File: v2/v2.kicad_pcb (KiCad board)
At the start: 2 copper layers, 10.6 x 5.5 mm, 63 parts, among them SW1 SW_Push, SW10 SW_Push, SW11 SW_Push, SW12 SW_Push, SW13 SW_Push, SW14 SW_Push, SW15 SW_Push, SW16 SW_Push, SW17 SW_Push, SW18 SW_Push, SW19 SW_Push, SW2 SW_Push, SW20 SW_Push, SW21 SW_Push, SW22 SW_Push, SW23 SW_Push, SW24 SW_Push, SW25 SW_Push, SW26 SW_Push, SW27 SW_Push, SW28 SW_Push, SW29 SW_Push, SW3 SW_Push, SW30 SW_Push, SW31 SW_Push, SW4 SW_Push, SW5 SW_Push, SW6 SW_Push, SW7 SW_Push, SW8 SW_Push, SW9 SW_Push

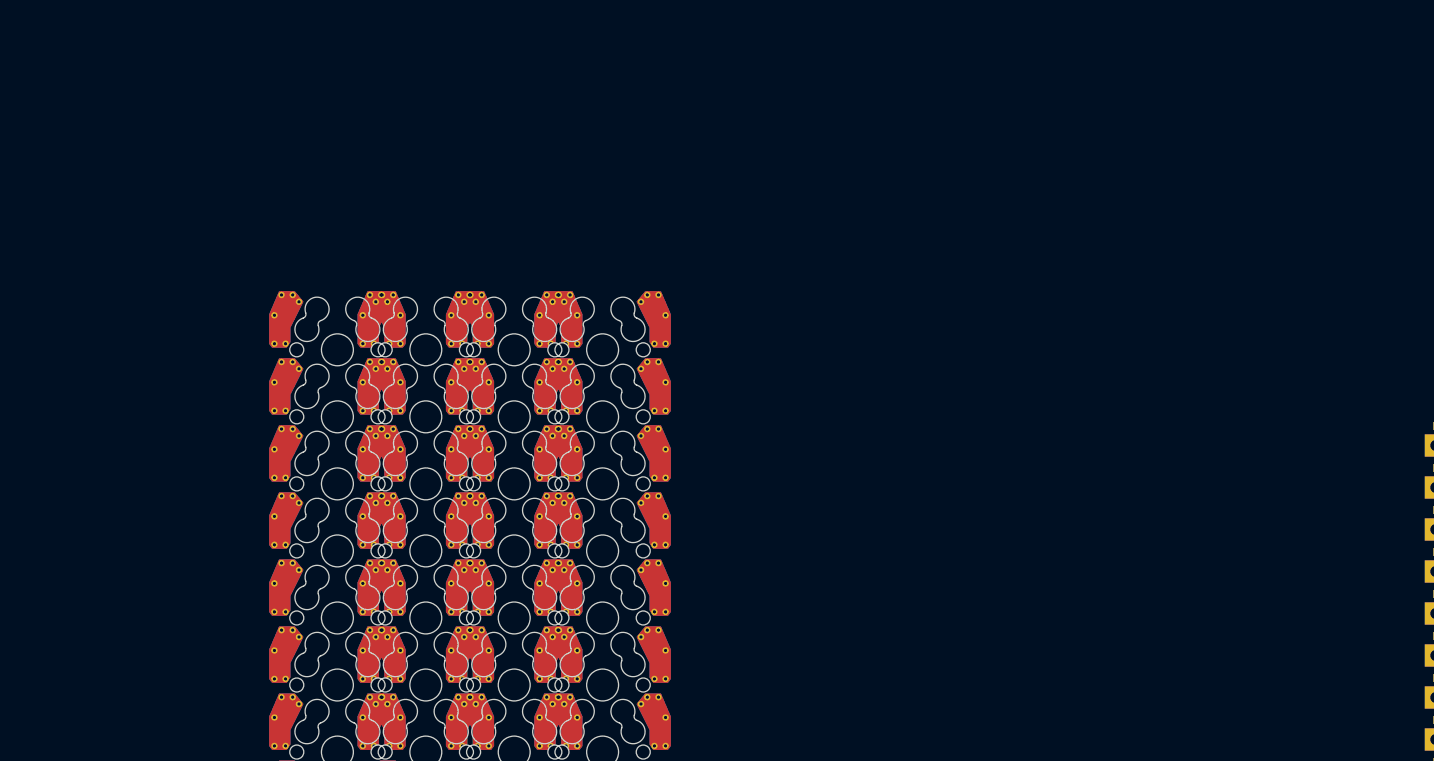
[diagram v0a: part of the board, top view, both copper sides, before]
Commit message: started adding backlighting
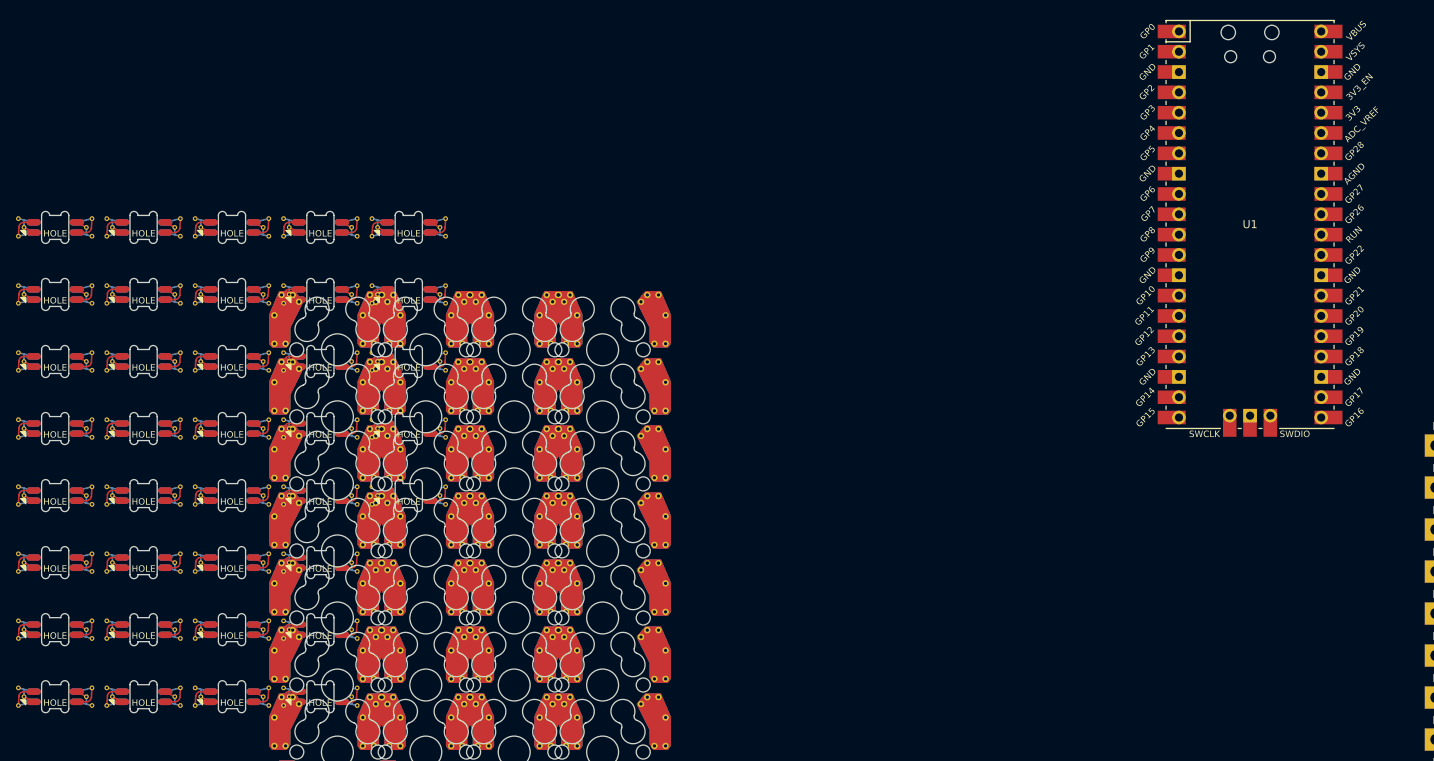
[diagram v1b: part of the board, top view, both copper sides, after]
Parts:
- added D33: SK6812MINI, reversible-kicad-footprints:MX-1U-SK6812Mini-E, F.Cu at (28.8, 34.7)
- added D34: SK6812MINI, reversible-kicad-footprints:MX-1U-SK6812Mini-E, F.Cu at (28.8, 43.0)
- added D35: SK6812MINI, reversible-kicad-footprints:MX-1U-SK6812Mini-E, F.Cu at (28.8, 51.4)
- added D36: SK6812MINI, reversible-kicad-footprints:MX-1U-SK6812Mini-E, F.Cu at (28.8, 59.8)
- added D37: SK6812MINI, reversible-kicad-footprints:MX-1U-SK6812Mini-E, F.Cu at (28.8, 68.2)
- added D38: SK6812MINI, reversible-kicad-footprints:MX-1U-SK6812Mini-E, F.Cu at (28.8, 76.6)
- added D39: SK6812MINI, reversible-kicad-footprints:MX-1U-SK6812Mini-E, F.Cu at (28.8, 84.9)
- added D40: SK6812MINI, reversible-kicad-footprints:MX-1U-SK6812Mini-E, F.Cu at (28.8, 93.3)
- added D41: SK6812MINI, reversible-kicad-footprints:MX-1U-SK6812Mini-E, F.Cu at (39.8, 34.7)
- added D42: SK6812MINI, reversible-kicad-footprints:MX-1U-SK6812Mini-E, F.Cu at (39.8, 43.0)
- added D43: SK6812MINI, reversible-kicad-footprints:MX-1U-SK6812Mini-E, F.Cu at (39.8, 51.4)
- added D44: SK6812MINI, reversible-kicad-footprints:MX-1U-SK6812Mini-E, F.Cu at (39.8, 59.8)
- added D45: SK6812MINI, reversible-kicad-footprints:MX-1U-SK6812Mini-E, F.Cu at (39.8, 68.2)
- added D46: SK6812MINI, reversible-kicad-footprints:MX-1U-SK6812Mini-E, F.Cu at (39.8, 76.6)
- added D47: SK6812MINI, reversible-kicad-footprints:MX-1U-SK6812Mini-E, F.Cu at (39.8, 84.9)
- added D48: SK6812MINI, reversible-kicad-footprints:MX-1U-SK6812Mini-E, F.Cu at (39.8, 93.3)
- added D49: SK6812MINI, reversible-kicad-footprints:MX-1U-SK6812Mini-E, F.Cu at (50.9, 34.7)
- added D50: SK6812MINI, reversible-kicad-footprints:MX-1U-SK6812Mini-E, F.Cu at (50.9, 43.0)
- added D51: SK6812MINI, reversible-kicad-footprints:MX-1U-SK6812Mini-E, F.Cu at (50.9, 51.4)
- added D52: SK6812MINI, reversible-kicad-footprints:MX-1U-SK6812Mini-E, F.Cu at (50.9, 59.8)
- added D53: SK6812MINI, reversible-kicad-footprints:MX-1U-SK6812Mini-E, F.Cu at (50.9, 68.2)
- added D54: SK6812MINI, reversible-kicad-footprints:MX-1U-SK6812Mini-E, F.Cu at (50.9, 76.6)
- added D55: SK6812MINI, reversible-kicad-footprints:MX-1U-SK6812Mini-E, F.Cu at (50.9, 84.9)
- added D56: SK6812MINI, reversible-kicad-footprints:MX-1U-SK6812Mini-E, F.Cu at (50.9, 93.3)
- added D57: SK6812MINI, reversible-kicad-footprints:MX-1U-SK6812Mini-E, F.Cu at (61.9, 34.7)
- added D58: SK6812MINI, reversible-kicad-footprints:MX-1U-SK6812Mini-E, F.Cu at (61.9, 43.0)
- added D59: SK6812MINI, reversible-kicad-footprints:MX-1U-SK6812Mini-E, F.Cu at (61.9, 51.4)
- added D60: SK6812MINI, reversible-kicad-footprints:MX-1U-SK6812Mini-E, F.Cu at (61.9, 59.8)
- added D61: SK6812MINI, reversible-kicad-footprints:MX-1U-SK6812Mini-E, F.Cu at (61.9, 68.2)
- added D62: SK6812MINI, reversible-kicad-footprints:MX-1U-SK6812Mini-E, F.Cu at (61.9, 76.6)
- added D63: SK6812MINI, reversible-kicad-footprints:MX-1U-SK6812Mini-E, F.Cu at (61.9, 84.9)
- added D64: SK6812MINI, reversible-kicad-footprints:MX-1U-SK6812Mini-E, F.Cu at (61.9, 93.3)
- added D65: SK6812MINI, reversible-kicad-footprints:MX-1U-SK6812Mini-E, F.Cu at (73.0, 34.7)
- added D66: SK6812MINI, reversible-kicad-footprints:MX-1U-SK6812Mini-E, F.Cu at (73.0, 43.0)
- added D67: SK6812MINI, reversible-kicad-footprints:MX-1U-SK6812Mini-E, F.Cu at (73.0, 51.4)
- added D68: SK6812MINI, reversible-kicad-footprints:MX-1U-SK6812Mini-E, F.Cu at (73.0, 59.8)
- added D69: SK6812MINI, reversible-kicad-footprints:MX-1U-SK6812Mini-E, F.Cu at (73.0, 68.2)
- added U1: Pico, RPi_Pico:RPi_Pico_SMD_TH, F.Cu at (178.1, 39.4)
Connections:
- D32 pad 1: unconnected-(D32-DOUT-Pad1) -> Net-(D32-DOUT)
- D32 pad 2: unconnected-(D32-VSS-Pad2) -> GND
- D32 pad 4: unconnected-(D32-VDD-Pad4) -> VBUS

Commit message: did some layout using a plugin
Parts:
- removed D36, D41, D47, D53, D59, D65: SK6812MINI, reversible-kicad-footprints:MX-1U-SK6812Mini-E
- added D28: D, Diode_THT:D_5W_P10.16mm_Horizontal, B.Cu at (195.1, 174.2)
- added SW28: SW_Push, reversible-kicad-footprints:MX-1U-Hotswap, F.Cu at (190.2, 169.2)
- D1: moved to B.Cu
- D10: renamed from D11; moved to B.Cu
- D11: renamed from D16; moved to B.Cu
- D12: renamed from D21; moved to B.Cu
- D13: renamed from D26; moved to B.Cu
- D14: renamed from D30; moved to B.Cu
- D15: renamed from D3; moved to B.Cu
- D16: renamed from D7; moved to B.Cu
- D17: renamed from D12; moved to B.Cu
- D18: renamed from D17; moved to B.Cu
- D19: renamed from D22; moved to B.Cu
- D2: renamed from D5; moved to B.Cu
- D20: renamed from D27; moved to B.Cu
- D21: renamed from D31; moved to B.Cu
- D22: renamed from D4; moved to B.Cu
- D23: renamed from D8; moved to B.Cu
- D24: renamed from D13; moved to B.Cu
- D25: renamed from D18; moved to B.Cu
- D26: renamed from D23; moved to B.Cu
- D27: renamed from D28; moved to B.Cu
- D29: renamed from D9; moved to B.Cu
- D3: renamed from D10; moved to B.Cu
- D30: renamed from D14; moved to B.Cu
- D31: renamed from D19; moved to B.Cu
- D32: renamed from D24; moved to B.Cu
- D4: renamed from D15; moved to B.Cu
- D5: renamed from D20; moved to B.Cu
- D6: renamed from D25; moved to B.Cu
- D7: renamed from D29; moved to B.Cu
- D8: renamed from D2; moved to B.Cu
- D9: renamed from D6; moved to B.Cu
- LED1: renamed from D32; moved to B.Cu
- LED10: renamed from D56; moved to B.Cu
- LED11: renamed from D50; moved to B.Cu
- LED12: renamed from D44; moved to B.Cu
- LED13: renamed from D38; moved to B.Cu
- LED14: renamed from D33; moved to B.Cu
- LED15: renamed from D34; moved to B.Cu
- LED16: renamed from D39; moved to B.Cu
- LED17: renamed from D45; moved to B.Cu
- LED18: renamed from D51; moved to B.Cu
- LED19: renamed from D57; moved to B.Cu
- LED2: renamed from D37; moved to B.Cu
- LED20: renamed from D63; moved to B.Cu
- LED21: renamed from D68; moved to B.Cu
- LED22: renamed from D69; moved to B.Cu
- LED23: renamed from D64; moved to B.Cu
- LED24: renamed from D58; moved to B.Cu
- LED25: renamed from D52; moved to B.Cu
- LED26: renamed from D46; moved to B.Cu
- LED27: renamed from D40; moved to B.Cu
- LED28: renamed from D35; moved to B.Cu
- LED29: renamed from D42; moved to B.Cu
- LED3: renamed from D43; moved to B.Cu
- LED30: renamed from D48; moved to B.Cu
- LED31: renamed from D54; moved to B.Cu
- LED32: renamed from D60; moved to B.Cu
- LED4: renamed from D49; moved to B.Cu
- LED5: renamed from D55; moved to B.Cu
- LED6: renamed from D61; moved to B.Cu
- LED7: renamed from D66; moved to B.Cu
- LED8: renamed from D67; moved to B.Cu
- LED9: renamed from D62; moved to B.Cu
- moved LED32 225.9 mm to (233.1, 207.2), turned to 149 degrees
- moved LED31 203.2 mm to (213.6, 198.3), turned to 159 degrees
- moved LED28 199.8 mm to (190.2, 169.2), turned to 179.5 degrees
- moved LED29 197.9 mm to (171.3, 190.9), turned to 174 degrees
- moved LED13 185.4 mm to (210.2, 114.7), turned to 179 degrees
- moved LED25 183.9 mm to (209.5, 152.8), turned to 179 degrees
- moved LED30 182.7 mm to (192.7, 193.4), turned to 169 degrees
- moved SW31 179.6 mm to (213.6, 198.3), turned to -21 degrees
- moved LED19 178.1 mm to (209.8, 133.7), turned to 179 degrees
- moved SW29 166.5 mm to (171.3, 190.9), turned to -6 degrees
- moved LED15 166.3 mm to (171.5, 128.5), turned to 179.5 degrees
- moved LED17 163.3 mm to (190.5, 131.1), turned to 179.5 degrees
- moved LED27 160.1 mm to (171.1, 166.6), turned to 179.5 degrees
- moved LED14 156.6 mm to (152.4, 130.8), turned to 179.5 degrees
- moved LED11 155.9 mm to (190.7, 112.0), turned to 179.5 degrees
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- renumbered SW11 to SW10, SW16 to SW11, SW21 to SW12, SW26 to SW13, SW30 to SW14, SW3 to SW15, SW7 to SW16, SW12 to SW17, SW17 to SW18, SW22 to SW19, SW5 to SW2, SW27 to SW20, SW31 to SW21, SW4 to SW22, SW8 to SW23, SW13 to SW24, SW18 to SW25, SW23 to SW26, SW28 to SW27, SW9 to SW29, SW10 to SW3, SW14 to SW30, SW19 to SW31, SW24 to SW32, SW15 to SW4, SW20 to SW5, SW25 to SW6, SW29 to SW7, SW2 to SW8, SW6 to SW9
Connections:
- LED22 pad 1: Net-(D36-DIN) -> Net-(LED22-DOUT)
- LED29 pad 1: Net-(D42-DOUT) -> unconnected-(LED29-DOUT-Pad1)
- LED29 pad 3: Net-(D42-DIN) -> Net-(LED22-DOUT)
- LED30 pad 1: Net-(D48-DOUT) -> unconnected-(LED30-DOUT-Pad1)
- LED30 pad 3: Net-(D42-DOUT) -> unconnected-(LED30-DIN-Pad3)
- LED31 pad 3: Net-(D48-DOUT) -> unconnected-(LED31-DIN-Pad3)
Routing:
- net Net-(D6-A): track 0.00 -> 6.31 mm
- net Net-(D31-A): track 0.00 -> 6.31 mm
- net Net-(D13-A): track 0.00 -> 6.31 mm
- net Net-(D30-A): track 0.00 -> 6.31 mm
- net Net-(D12-A): track 0.00 -> 6.31 mm
- net Net-(D24-A): track 0.00 -> 6.31 mm
- net Net-(D7-A): track 0.00 -> 6.31 mm
- net Net-(D18-A): track 0.00 -> 6.31 mm
- net Net-(D9-A): track 0.00 -> 6.31 mm
- net Net-(D25-A): track 0.00 -> 6.31 mm
- net Net-(D4-A): track 0.00 -> 6.31 mm
- net Net-(D11-A): track 0.00 -> 6.31 mm
- net Net-(D32-A): track 0.00 -> 6.31 mm
- net Net-(D29-A): track 0.00 -> 6.31 mm
- net Net-(D19-A): track 0.00 -> 6.31 mm
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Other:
- board size 10.6 x 5.5 mm -> 9.7 x 8.4 mm

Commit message: schematic finished + some pcb
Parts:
- added D33: D, Diode_THT:D_5W_P10.16mm_Horizontal, F.Cu at (224.7, 186.4)
- added J1: Conn_01x04_Pin, Keebio-Parts:I2C_Breakout, F.Cu at (244.6, 150.5)
- added J2: Conn_01x04_Pin, Keebio-Parts:I2C_Breakout, B.Cu at (225.5, 150.5)
- added J3: Conn_01x04_Pin, Keebio-Parts:TRRS-PJ-320A-dual, F.Cu at (248.5, 176.5)
- added R1: 5K, Keebio-Parts:Resistor, F.Cu at (226.0, 162.9)
- added R2: 5K, Keebio-Parts:Resistor, F.Cu at (221.5, 161.5)
- added R3: 5K (LEFT), Keebio-Parts:Resistor, F.Cu at (229.5, 164.0)
- added R4: 5K (RIGHT), Keebio-Parts:Resistor, F.Cu at (233.0, 165.0)
- added SW33: RotaryEncoder_Switch, Keebio-Parts:RotaryEncoder_EC11, F.Cu at (216.0, 176.4)
- added U2: Pico, Module:RaspberryPi_Pico_SMD_HandSolder, B.Cu at (235.1, 120.0)
- U1: footprint RPi_Pico:RPi_Pico_SMD_TH -> Module:RaspberryPi_Pico_SMD_HandSolder
- moved U1 8.59 mm to (235.1, 120.0)
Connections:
- D29 pad 1: Net-(D29-K) -> Row 5
- D30 pad 1: Net-(D29-K) -> Row 5
- D31 pad 1: Net-(D29-K) -> Row 5
- D32 pad 1: Net-(D29-K) -> Row 5
- LED1 pad 3: unconnected-(LED1-DIN-Pad3) -> SK6912PWM
- U1 pad 1: unconnected-(U1-GPIO0-Pad1) -> Col 1
- U1 pad 10: unconnected-(U1-GPIO7-Pad10) -> Row 1
- U1 pad 11: unconnected-(U1-GPIO8-Pad11) -> Row 2
- U1 pad 12: unconnected-(U1-GPIO9-Pad12) -> Row 3
- U1 pad 13: unconnected-(U1-GND-Pad13) -> Row 4
- U1 pad 14: unconnected-(U1-GPIO10-Pad14) -> Row 5
- U1 pad 2: unconnected-(U1-GPIO1-Pad2) -> Col 2
- U1 pad 21: unconnected-(U1-GPIO16-Pad21) -> SPLIT SELECT
- U1 pad 24: unconnected-(U1-GPIO18-Pad24) -> SERIAL B
- U1 pad 25: unconnected-(U1-GPIO19-Pad25) -> SERIAL A
- U1 pad 39: unconnected-(U1-VSYS-Pad39) -> VSYS
- U1 pad 4: unconnected-(U1-GPIO2-Pad4) -> Col 3
- U1 pad 5: unconnected-(U1-GPIO3-Pad5) -> Col 4
- U1 pad 6: unconnected-(U1-GPIO4-Pad6) -> Col 5
- U1 pad 7: unconnected-(U1-GPIO5-Pad7) -> Col 6
- U1 pad 9: unconnected-(U1-GPIO6-Pad9) -> Col 7
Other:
- board size 9.7 x 8.4 mm -> 166.3 x 141.5 mm

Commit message: I screwed up some layout
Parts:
- removed R1, R2: 5K, Keebio-Parts:Resistor
- D1, D10, D11, D12, D13, D14, D15, D16, D17, D18, D19, D2, D20, D21, D22, D23, D24, D25, D26, D27, D28, D29, D3, D30, D31, D32, D4, D5, D6, D7, D8, D9: footprint Diode_THT:D_5W_P10.16mm_Horizontal -> Keebio-Parts:Diode-Hybrid-Back; moved to F.Cu
- D33: footprint Diode_THT:D_5W_P10.16mm_Horizontal -> Keebio-Parts:Diode-Hybrid-Back
- J2, LED1, LED10, LED11, LED12, LED13, LED14, LED15, LED16, LED17, LED18, LED19, LED2, LED20, LED21, LED22, LED23, LED24, LED25, LED26, LED27, LED28, LED29, LED3, LED30, LED31, LED32, LED4, LED5, LED6, LED7, LED8, LED9, U2: moved to F.Cu
- moved SW32 230.8 mm to (63.2, 51.0), turned to 0 degrees
- moved SW31 217.9 mm to (63.2, 40.7), turned to 0 degrees
- moved D7 215.2 mm to (2.12, 128.9), turned to 0 degrees
- moved D32 215.2 mm to (31.1, 144.7), turned to 0 degrees
- moved J3 209.1 mm to (49.4, 112.6), turned to 0 degrees
- moved SW30 208.2 mm to (63.2, 30.4), turned to 0 degrees
- moved SW19 206.2 mm to (45.1, 9.70), turned to 0 degrees
- moved SW28 203.9 mm to (63.2, 9.70), turned to 0 degrees
- moved SW29 202.2 mm to (63.2, 20.0), turned to 0 degrees
- moved J1 200.1 mm to (45.8, 127.9), turned to 0 degrees
- moved D13 199.2 mm to (16.6, 102.7), turned to 0 degrees
- moved D19 198.2 mm to (16.6, 134.2), turned to 0 degrees
- moved D33 196.9 mm to (31.1, 149.9), turned to 0 degrees
- moved D31 196.5 mm to (31.1, 139.4), turned to 0 degrees
- moved D11 196.3 mm to (2.12, 149.9), turned to 0 degrees
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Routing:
- net Net-(D6-A): track 6.31 -> 0.00 mm
- net Net-(D31-A): track 6.31 -> 0.00 mm
- net Net-(D13-A): track 6.31 -> 0.00 mm
- net Net-(D30-A): track 6.31 -> 0.00 mm
- net Net-(D12-A): track 6.31 -> 0.00 mm
- net Net-(D24-A): track 6.31 -> 0.00 mm
- net Net-(D7-A): track 6.31 -> 0.00 mm
- net Net-(D18-A): track 6.31 -> 0.00 mm
- net Net-(D9-A): track 6.31 -> 0.00 mm
- net Net-(D25-A): track 6.31 -> 0.00 mm
- net Net-(D4-A): track 6.31 -> 0.00 mm
- net Net-(D11-A): track 6.31 -> 0.00 mm
- net Net-(D32-A): track 6.31 -> 0.00 mm
- net Net-(D29-A): track 6.31 -> 0.00 mm
- net Net-(D19-A): track 6.31 -> 0.00 mm
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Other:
- board size 166.3 x 141.5 mm -> 10.3 x 7.2 mm

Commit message: layout fix started
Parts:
- moved SW15 67.3 mm to (163.5, 105.2), turned to -15 degrees
- moved SW16 61.3 mm to (187.4, 111.6), turned to -15 degrees
- moved SW17 60.7 mm to (206.2, 116.7), turned to -15.5 degrees
- moved SW14 58.3 mm to (266.9, 116.1), turned to -16 degrees

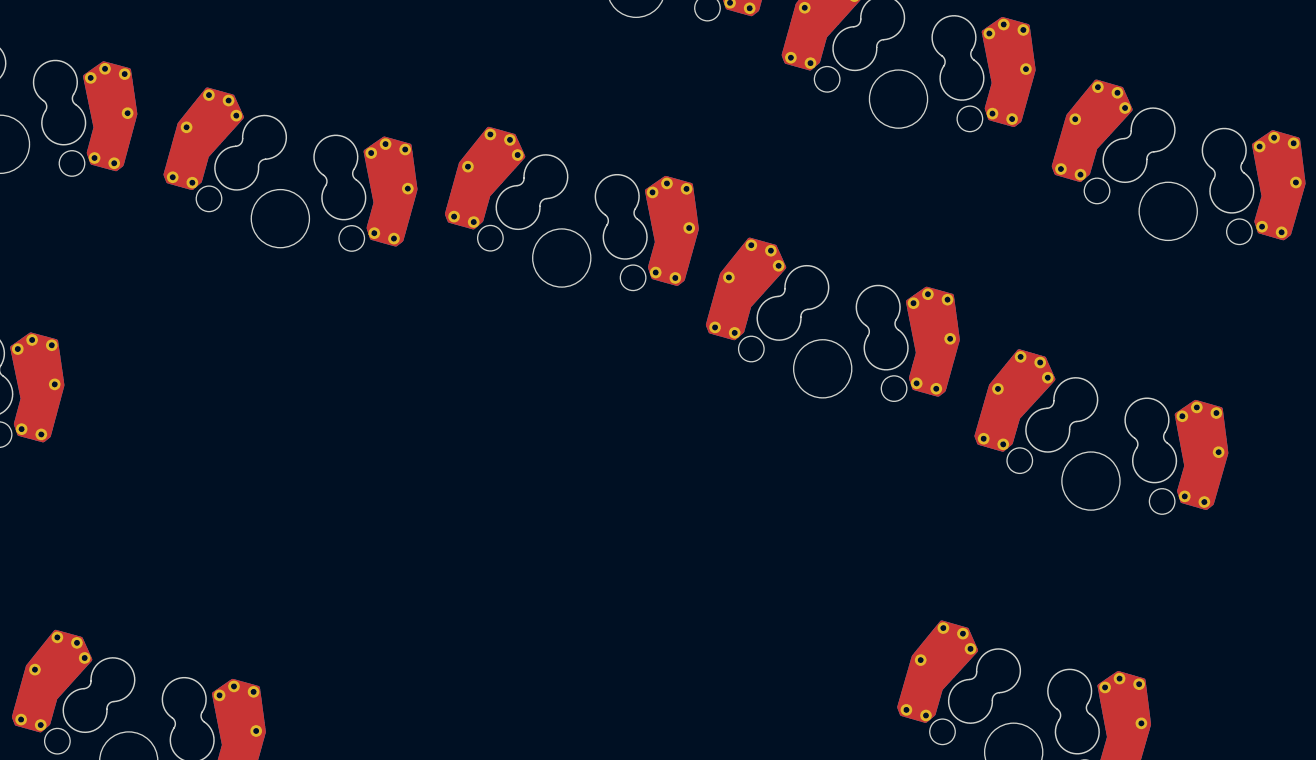
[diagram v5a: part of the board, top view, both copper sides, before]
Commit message: started moving some of the keys into place
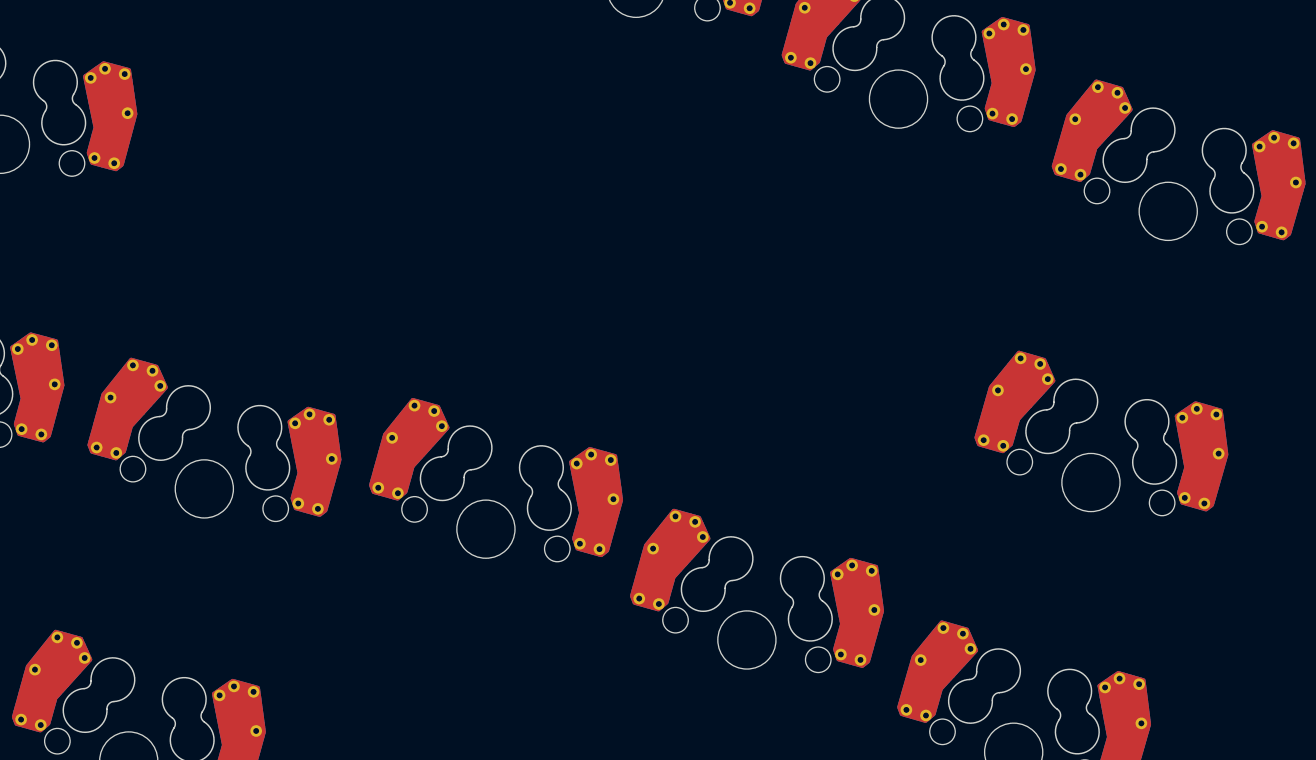
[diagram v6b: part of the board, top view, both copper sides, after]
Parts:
- moved SW9 67.5 mm to (168.5, 86.6), turned to -15 degrees
- moved SW12 63.8 mm to (230.7, 100.8), turned to -15.5 degrees
- moved SW10 61.5 mm to (192.4, 93.0), turned to -15 degrees
- moved SW11 60.8 mm to (211.4, 98.0), turned to -15.5 degrees
- moved SW8 58.5 mm to (272.2, 97.6), turned to -16 degrees
- moved SW13 58.3 mm to (248.6, 108.4), turned to -15.5 degrees
